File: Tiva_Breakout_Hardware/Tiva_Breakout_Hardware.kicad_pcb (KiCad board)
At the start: 2 copper layers, 139.8 x 79.5 mm, 7 parts, among them U1 TM4C129E_Launchpad

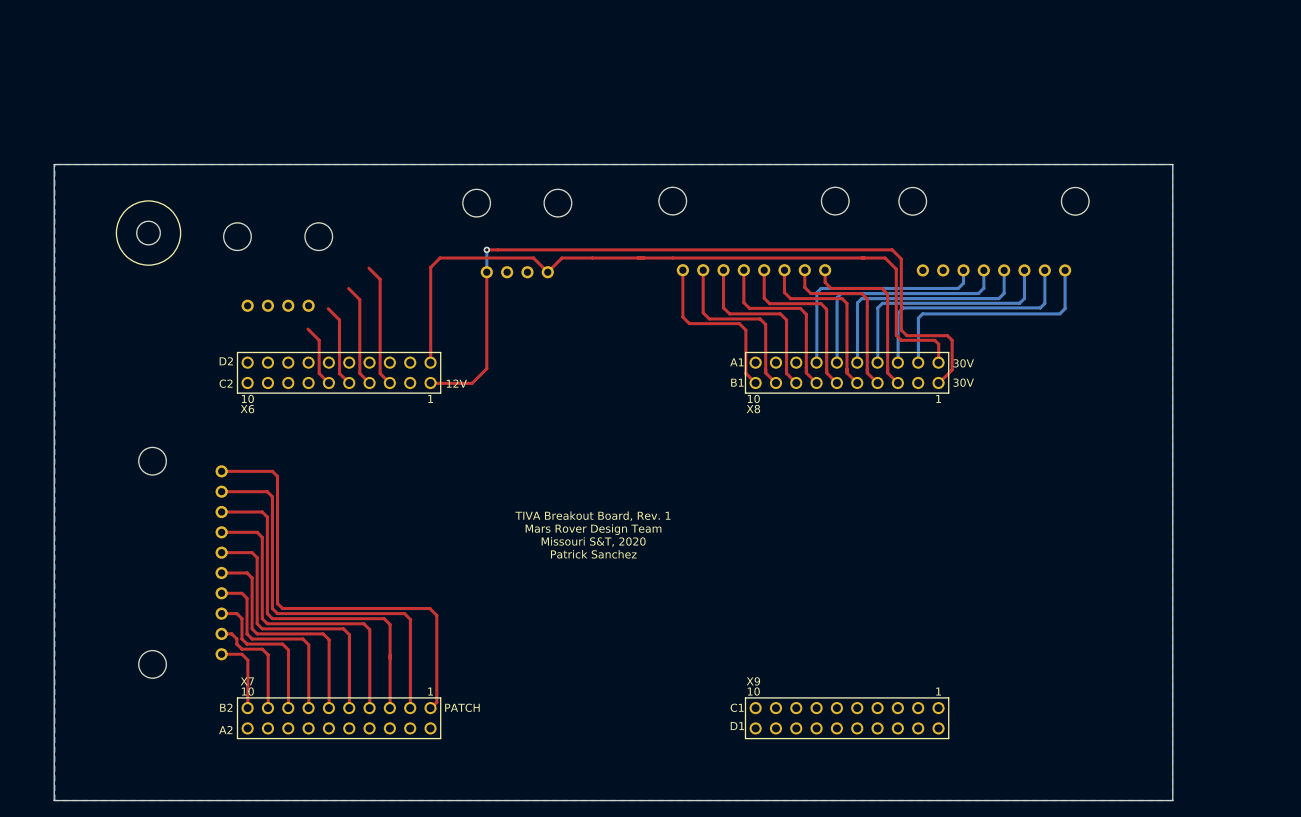
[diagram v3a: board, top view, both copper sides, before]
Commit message: New layout, as board is on left of others now. Changed pin assignments.
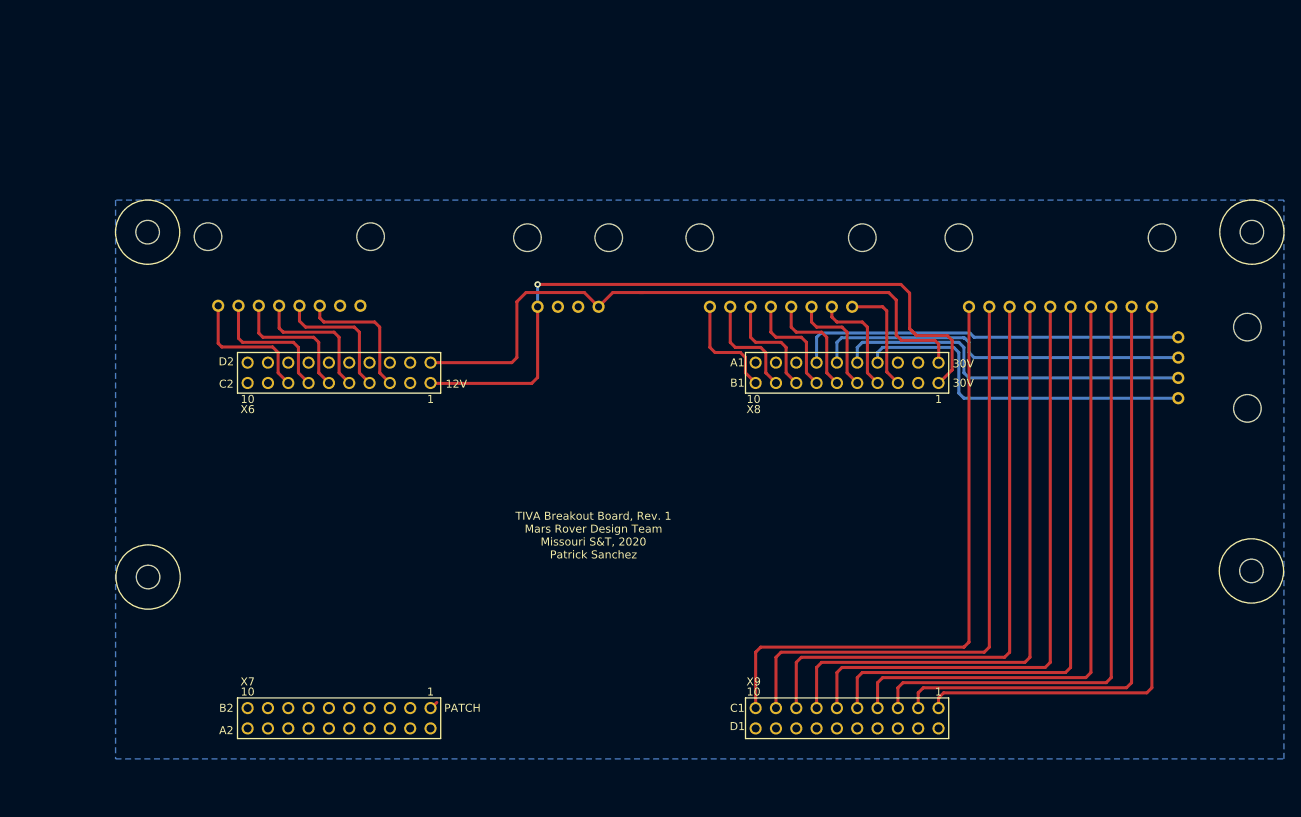
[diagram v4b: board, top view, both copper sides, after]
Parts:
- removed the REF** at (92.7, 83.4)
- added REF**: 4_40_Hole, MRDT_Drill_Holes:4_40_Hole, F.Cu at (88.6, 122.4)
- added REF**: 4_40_Hole, MRDT_Drill_Holes:4_40_Hole, F.Cu at (226.5, 121.7)
- added REF**: 4_40_Hole, MRDT_Drill_Holes:4_40_Hole_Corner, F.Cu at (230.6, 75.3)
- added REF**: 4_40_Hole, MRDT_Drill_Holes:4_40_Hole_Corner, F.Cu at (84.5, 75.3)
- moved 12V_B2 112.8 mm to (217.4, 96.3), turned to 90 degrees
- moved ConnPCH_C2 109.6 mm to (202.6, 88.6), turned to 180 degrees
- moved Conn30V_L1 88.2 mm to (106.2, 88.5)
- moved ConnIN1 7.68 mm to (141.1, 88.6)
- moved Conn30V_R1 5.68 mm to (167.7, 88.6)
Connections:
- U1 pad PB4: Net-(12V_B2-Pad1) -> Net-(Conn30V_L1-Pad3)
- U1 pad PB5: Net-(12V_B2-Pad2) -> Net-(Conn30V_L1-Pad4)
- U1 pad PC4: Net-(Conn30V_L1-Pad2) -> Net-(U1-PadPC4)
- U1 pad PC5: Net-(Conn30V_L1-Pad3) -> Net-(12V_B2-Pad1)
- U1 pad PC6: Net-(Conn30V_L1-Pad4) -> Net-(12V_B2-Pad2)
- U1 pad PD3: Net-(Conn30V_L1-Pad6) -> Net-(12V_B2-Pad4)
- U1 pad PE4: Net-(Conn30V_L1-Pad1) -> Net-(U1-PadPE4)
- U1 pad PE5: Net-(Conn30V_L1-Pad5) -> Net-(12V_B2-Pad3)
- U1 pad PF1: Net-(U1-PadPF1) -> Net-(ConnPCH_C2-Pad1)
- U1 pad PF2: Net-(U1-PadPF2) -> Net-(ConnPCH_C2-Pad2)
- U1 pad PF3: Net-(U1-PadPF3) -> Net-(ConnPCH_C2-Pad3)
- U1 pad PG0: Net-(U1-PadPG0) -> Net-(ConnPCH_C2-Pad4)
- U1 pad PG1: Net-(ConnPCH_C2-Pad1) -> Net-(U1-PadPG1)
- U1 pad PH0: Net-(ConnPCH_C2-Pad7) -> Net-(U1-PadPH0)
- U1 pad PH1: Net-(ConnPCH_C2-Pad8) -> Net-(U1-PadPH1)
- U1 pad PK0: Net-(12V_B2-Pad3) -> Net-(Conn30V_L1-Pad5)
- U1 pad PK1: Net-(12V_B2-Pad4) -> Net-(Conn30V_L1-Pad6)
- U1 pad PK2: Net-(U1-PadPK2) -> Net-(Conn30V_L1-Pad7)
- U1 pad PK3: Net-(U1-PadPK3) -> Net-(Conn30V_L1-Pad8)
- U1 pad PK4: Net-(ConnPCH_C2-Pad2) -> Net-(U1-PadPK4)
- U1 pad PK5: Net-(ConnPCH_C2-Pad3) -> Net-(U1-PadPK5)
- U1 pad PK6: Net-(ConnPCH_C2-Pad9) -> Net-(U1-PadPK6)
- U1 pad PK7: Net-(ConnPCH_C2-Pad10) -> Net-(U1-PadPK7)
- U1 pad PL0: Net-(U1-PadPL0) -> Net-(ConnPCH_C2-Pad7)
- U1 pad PL1: Net-(U1-PadPL1) -> Net-(ConnPCH_C2-Pad8)
- U1 pad PL2: Net-(U1-PadPL2) -> Net-(ConnPCH_C2-Pad9)
- U1 pad PL3: Net-(U1-PadPL3) -> Net-(ConnPCH_C2-Pad10)
- U1 pad PL4: Net-(U1-PadPL4) -> Net-(ConnPCH_C2-Pad5)
- U1 pad PL5: Net-(U1-PadPL5) -> Net-(ConnPCH_C2-Pad6)
- U1 pad PM0: Net-(ConnPCH_C2-Pad4) -> Net-(U1-PadPM0)
- U1 pad PM1: Net-(ConnPCH_C2-Pad5) -> Net-(U1-PadPM1)
- U1 pad PM2: Net-(ConnPCH_C2-Pad6) -> Net-(U1-PadPM2)
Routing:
- net Net-(ConnPCH_C2-Pad10): track 9.63 -> 76.1 mm
- net Net-(ConnPCH_C2-Pad9): track 14.0 -> 76.1 mm
- net Net-(ConnPCH_C2-Pad8): track 19.0 -> 76.1 mm
- net Net-(ConnPCH_C2-Pad7): track 24.1 -> 76.1 mm
- net Net-(ConnPCH_C2-Pad6): track 29.2 -> 76.1 mm
- net Net-(ConnPCH_C2-Pad5): track 34.3 -> 76.1 mm
- net Net-(12V_B2-Pad4): track 7.88 -> 48.8 mm
- net Net-(ConnPCH_C2-Pad4): track 39.4 -> 76.1 mm
- net Net-(12V_B2-Pad3): track 10.7 -> 47.2 mm
- net Net-(12V_B2-Pad2): track 13.0 -> 46.0 mm
- net Net-(ConnPCH_C2-Pad3): track 44.9 -> 76.1 mm
- net Net-(12V_B2-Pad1): track 15.5 -> 44.7 mm
- net Net-(Conn30V_L1-Pad1): track 29.2 -> 0.00 mm
- net Net-(Conn30V_L1-Pad2): track 29.2 -> 0.00 mm
- net Net-(ConnPCH_C2-Pad2): track 49.5 -> 76.1 mm
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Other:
- board outline removed

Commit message: Corrected schematic to match 30V board
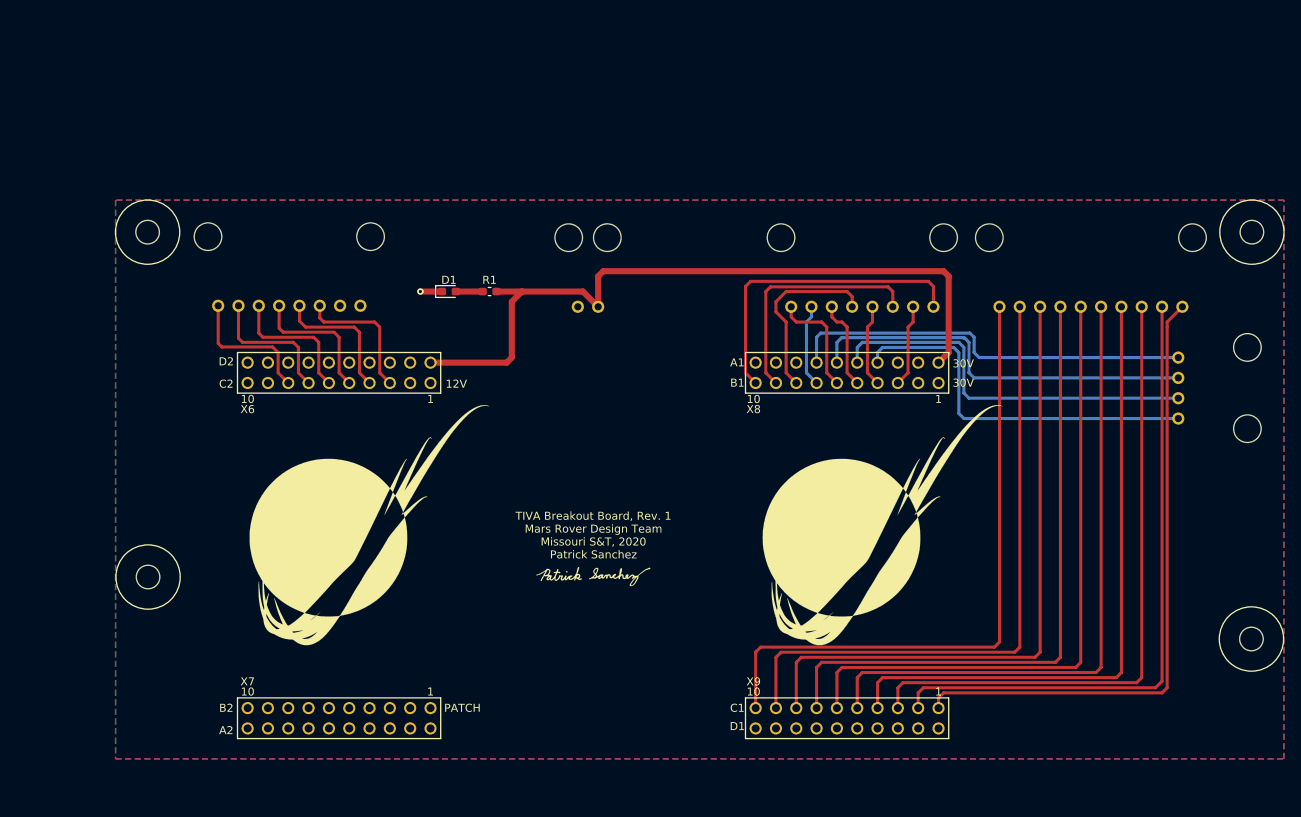
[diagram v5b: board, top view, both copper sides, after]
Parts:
- removed ConnIN1: Molex_SL_04, MRDT_Connectors:MOLEX_SL_04_Horizontal
- added Conn1: Molex_SL_02, MRDT_Connectors:MOLEX_SL_02_Horizontal, B.Cu at (143.6, 88.6)
- added D1: 3V3_LED, LED_SMD:LED_0603_1608Metric_Pad1.05x0.95mm_HandSolder, F.Cu at (126.2, 86.7)
- added G***: LOGO, MRDT_Silkscreens:0_MRDT_Logo_30mm, F.Cu at (180.4, 116.0)
- added G***: LOGO, MRDT_Silkscreens:0_MRDT_Logo_30mm, F.Cu at (116.3, 116.0)
- added G***: LOGO, MRDT_Silkscreens:z_sig_Patrick_Sanchez_15mmx5mm, F.Cu at (144.2, 122.3)
- added R1: 330, Resistor_SMD:R_0603_1608Metric_Pad1.05x0.95mm_HandSolder, F.Cu at (131.3, 86.7)
- moved Conn30V_R1 10.2 mm to (177.9, 88.6)
- moved REF** 8.51 mm to (226.5, 130.2)
- moved ConnPCH_C2 3.81 mm to (206.5, 88.6)
- moved 12V_B2 2.54 mm to (217.4, 98.8)
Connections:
- Conn30V_R1 pad 1: Net-(Conn30V_R1-Pad1) -> EX_ON
- Conn30V_R1 pad 2: Net-(Conn30V_R1-Pad2) -> EX_CURR
- Conn30V_R1 pad 3: Net-(Conn30V_R1-Pad3) -> 12V_ON
- Conn30V_R1 pad 4: Net-(Conn30V_R1-Pad4) -> 12V_CURR
- Conn30V_R1 pad 5: Net-(Conn30V_R1-Pad5) -> AUX_ON
- Conn30V_R1 pad 6: Net-(Conn30V_R1-Pad6) -> AUX_CURR
- Conn30V_R1 pad 7: Net-(Conn30V_R1-Pad7) -> RKT_ON
- Conn30V_R1 pad 8: Net-(Conn30V_R1-Pad8) -> RKT_CURR
- U1 pad +5V: +5VA -> Net-(U1-Pad+5V)
- U1 pad +5V': +5VA -> Net-(U1-Pad+5V')
- U1 pad PA6: Net-(Conn30V_R1-Pad6) -> AUX_ON
- U1 pad PD7: Net-(Conn30V_R1-Pad5) -> RKT_ON
- U1 pad PE0: Net-(Conn30V_R1-Pad1) -> EX_CURR
- U1 pad PE1: Net-(Conn30V_R1-Pad2) -> 12V_CURR
- U1 pad PE2: Net-(Conn30V_R1-Pad3) -> AUX_CURR
- U1 pad PE3: Net-(Conn30V_R1-Pad4) -> RKT_CURR
- U1 pad PM4: Net-(Conn30V_R1-Pad7) -> 12V_ON
- U1 pad PM5: Net-(Conn30V_R1-Pad8) -> EX_ON
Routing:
- net +5VA: track 89.6 -> 0.00 mm, vias 1 -> 0
- net EX_ON: track 0.00 -> 39.2 mm
- net 12V_ON: track 0.00 -> 30.2 mm
- net AUX_ON: track 0.00 -> 22.8 mm
- net Net-(Conn30V_R1-Pad1): track 14.1 -> 0.00 mm
- net Net-(Conn30V_R1-Pad8): track 13.8 -> 0.00 mm
- net Net-(Conn30V_R1-Pad5): track 13.8 -> 0.00 mm
- net Net-(Conn30V_R1-Pad4): track 13.8 -> 0.00 mm
- net RKT_CURR: track 0.00 -> 13.8 mm
- net Net-(Conn30V_R1-Pad2): track 13.8 -> 0.00 mm
- net Net-(Conn30V_R1-Pad3): track 13.8 -> 0.00 mm
- net Net-(Conn30V_R1-Pad7): track 13.8 -> 0.00 mm
- net Net-(Conn30V_R1-Pad6): track 13.8 -> 0.00 mm
- net +3V3: track 80.8 -> 92.2 mm
- net AUX_CURR: track 0.00 -> 11.2 mm
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- added copper zone on F.Cu, net GND
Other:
- board text removed: "+5V"

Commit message: Ready for CDR
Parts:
- Conn30V_L1: value Molex_SL_08 -> Molex_SL_07; footprint MRDT_Connectors:MOLEX_SL_08_Horizontal -> MRDT_Connectors:MOLEX_SL_07_Horizontal
- moved Conn30V_L1 1.27 mm to (105.0, 88.5)
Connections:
- Conn1 pad 1: +3V3 -> GND
- Conn1 pad 2: GND -> +3V3
- U1 pad PB4: Net-(Conn30V_L1-Pad3) -> Net-(Conn30V_L1-Pad2)
- U1 pad PB5: Net-(Conn30V_L1-Pad4) -> Net-(Conn30V_L1-Pad3)
- U1 pad PK0: Net-(Conn30V_L1-Pad5) -> Net-(Conn30V_L1-Pad4)
- U1 pad PK1: Net-(Conn30V_L1-Pad6) -> Net-(Conn30V_L1-Pad5)
- U1 pad PK2: Net-(Conn30V_L1-Pad7) -> Net-(Conn30V_L1-Pad6)
- U1 pad PK3: Net-(Conn30V_L1-Pad8) -> Net-(Conn30V_L1-Pad7)
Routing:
- net Net-(Conn30V_L1-Pad8): track 17.0 -> 0.00 mm
- net Net-(Conn30V_L1-Pad2): track 0.00 -> 17.0 mm
- net +3V3: track 92.2 -> 92.8 mm
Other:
- board outline added: 146.1 x 69.8 mm
- board text added: "12V_CURR"
- board text added: "12V_ON"
- board text added: "30V_L"
- board text added: "30V_R"
- board text added: "3V3_LED"
- board text added: "AUX_CURR"
- board text added: "AUX_ON"
- board text added: "EX_CURR"
- board text added: "EX_ON"
- board text added: "M1_CURR"
- board text added: "M1_ON"
- board text added: "M2_CURR"
- board text added: "M2_ON"
- board text added: "M3_CURR"
- board text added: "M3_ON"
- board text added: "PATCH PANEL"
- board text added: "PCH_1"
- board text added: "PCH_2"
- board text added: "PCH_3"
- board text added: "PCH_4"
- board text added: "PCH_5"
- board text added: "PCH_6"
- board text added: "PCH_7"
- board text added: "PCH_8"
- board text added: "RKT_CURR"
- board text added: "RKT_ON"
- board text added: "TEST_LED1"
- board text added: "TEST_LED2"
